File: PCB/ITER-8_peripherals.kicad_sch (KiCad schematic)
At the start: 8 parts

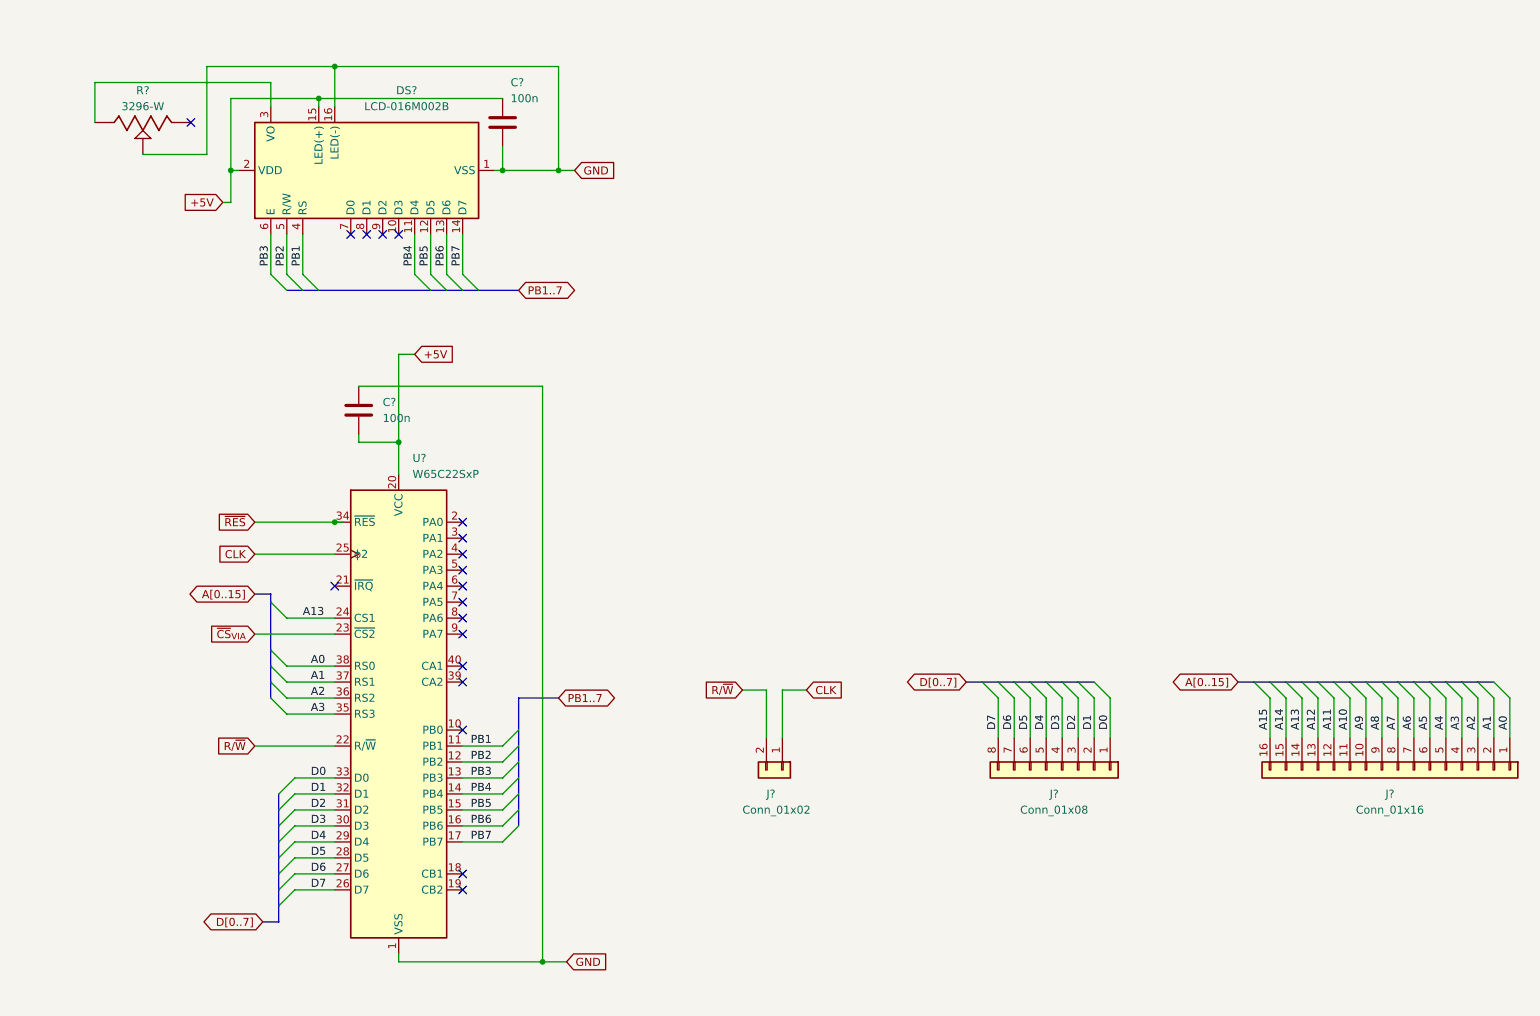
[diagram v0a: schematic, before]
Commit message: Button interrupt
New test to count the number of interrupts from a push button. The power section has been changed to automatically reset the computer.
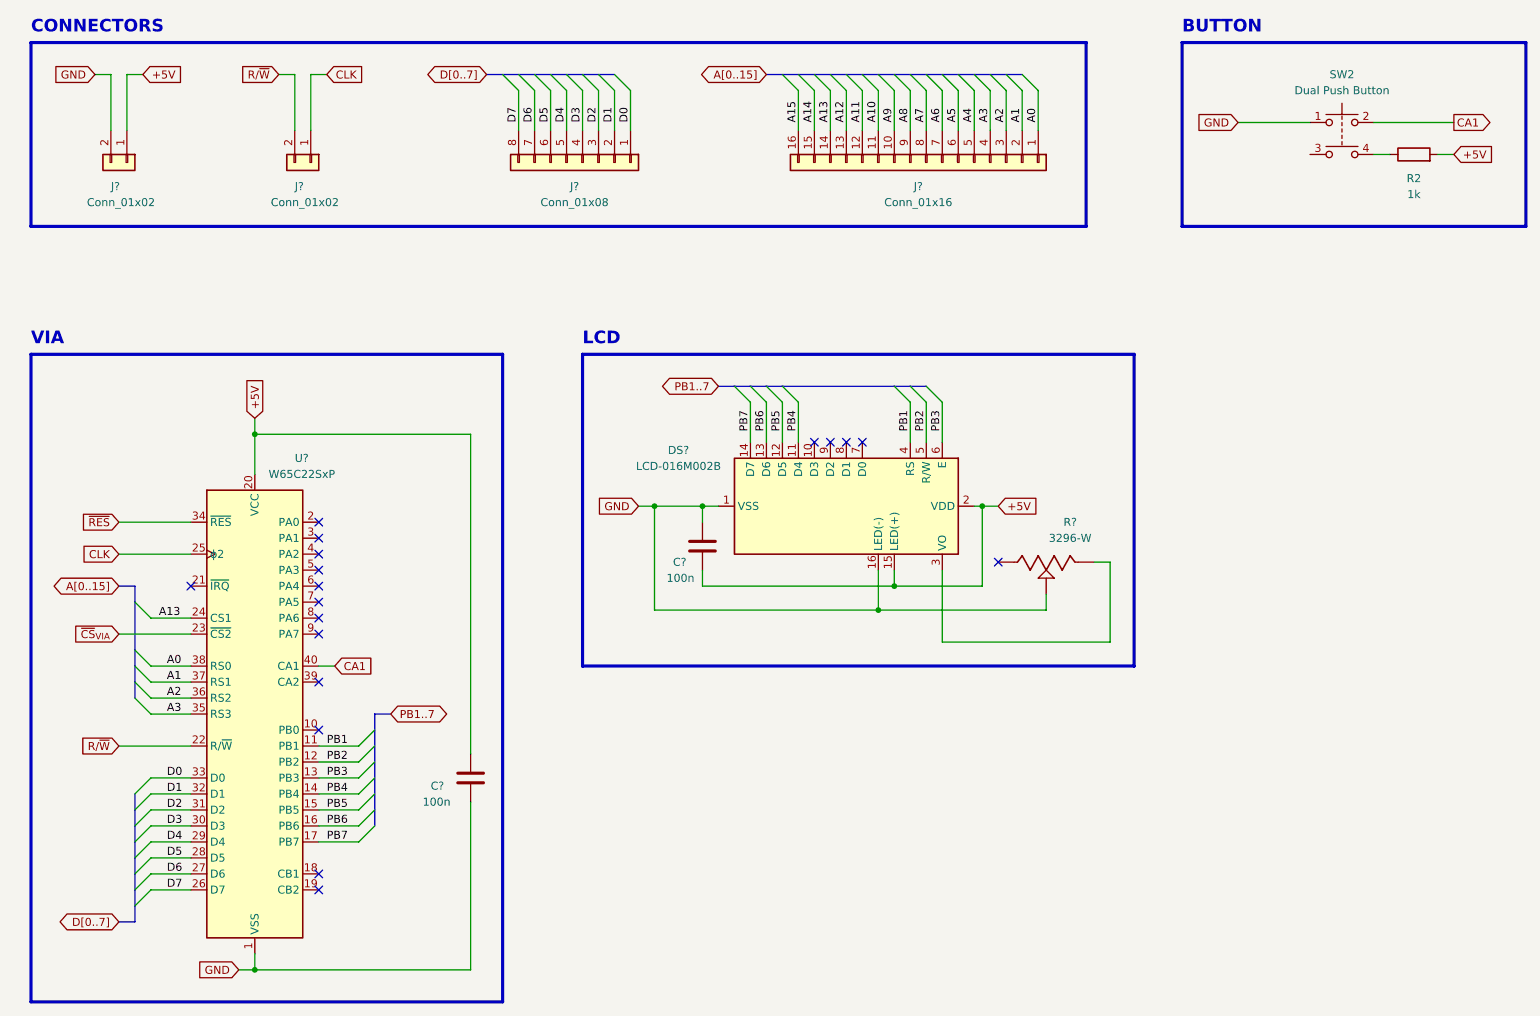
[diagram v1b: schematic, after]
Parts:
- added J?: Conn_01x02, Connector_PinSocket_2.54mm:PinSocket_1x02_P2.54mm_Vertical, symbol Connector_Generic:Conn_01x02
- added R2: 1k, Resistor_THT:R_Axial_DIN0207_L6.3mm_D2.5mm_P10.16mm_Horizontal, symbol Device:R
- added SW2: Dual Push Button, My footprints:SW_PUSH_double_6mm, symbol Switch:SW_Push_Dual
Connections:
- net +5V: now also J?.1 (Pin_1), R2.2
- net GND: now also J?.2 (Pin_2), SW2.1
- net CA1: now reaches U?.40 (CA1)
- net CA1: now also SW2.2
- new net: R2.1, SW2.4
- no-connect marks 19 -> 18
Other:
- note added: "BUTTON"
- note added: "CONNECTORS"
- note added: "LCD"
- note added: "VIA"
- moved on the sheet: C?, DS?, J?, R?, U?
